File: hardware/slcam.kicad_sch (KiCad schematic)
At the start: 36 parts, among them J1 532610671, J2 Conn_01x08, J3 Conn_01x04, J4 532610371, J5 532610371, U1 STM32F103C8Tx, U2 W25Q128JVS, U3 TCAN330G, U4 TPS2044D, Y1 Crystal_GND24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

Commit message: hardware: Fixing the footprint of the 32 kHz crystal #45
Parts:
- Y2: footprint lib:ECS-.327-12.5-34R-C-TR -> Crystal:Crystal_SMD_MicroCrystal_CC7V-T1A-2Pin_3.2x1.5mm_HandSoldering
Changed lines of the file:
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@@
     (property "Reference" "Y2" (id 0) (at 112.776 118.11 0))
     (property "Value" "Crystal" (id 1) (at 112.776 120.65 0))
-    (property "Footprint" "lib:ECS-.327-12.5-34R-C-TR" (id 2) (at 112.776 125.73 0)
+    (property "Footprint" "Crystal:Crystal_SMD_MicroCrystal_CC7V-T1A-2Pin_3.2x1.5mm_HandSoldering" (id 2) (at 112.776 125.73 0)
       (effects (font (size 1.27 1.27)) hide)
     )
@@
     )
     (path "/c55ccd54-28af-4ab4-883e-eafa97dc9bf8"
-      (reference "Y2") (unit 1) (value "Crystal") (footprint "lib:ECS-.327-12.5-34R-C-TR")
-    )
-  )
+      (reference "Y2") (unit 1) (value "Crystal") (footprint "Crystal:Crystal_SMD_MicroCrystal_CC7V-T1A-2Pin_3.2x1.5mm_HandSoldering")
+    )
+  )

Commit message: hardware: schematics: Adding the partnumbers of some components #52
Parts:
- D1: Partnumber (none) -> LTST-C171GKT
- D2: Partnumber (none) -> LTST-C170KFKT
- J1: Partnumber (none) -> 53261-0671
- J4, J5: Partnumber (none) -> 53261-0371
- U1: Partnumber (none) -> STM32F103C8T6
- U2: Partnumber (none) -> W25Q128JVSIM TR
- U3: Partnumber (none) -> TCAN330GD
- U4: Partnumber (none) -> TPS2044D
- Y1: Partnumber (none) -> ECS-80-10-33-CHN-TR3
- Y2: Partnumber (none) -> ECS-.327-12.5-34S-TR
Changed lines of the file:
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@@
+      (effects (font (size 1.27 1.27)) hide)
+    )
+    (property "Partnumber" "STM32F103C8T6" (id 4) (at 49.53 101.6 0)
       (effects (font (size 1.27 1.27)) hide)
     )
@@
       (effects (font (size 1.27 1.27)) hide)
     )
+    (property "Partnumber" "W25Q128JVSIM TR" (id 4) (at 53.34 248.92 0)
+      (effects (font (size 1.27 1.27)) hide)
+    )
     (pin "1")
     (pin "2")
@@
     )
     (property "Datasheet" "http://www.ti.com/lit/ds/symlink/tps2044.pdf" (id 3) (at 172.72 44.45 0)
+      (effects (font (size 1.27 1.27)) hide)
+    )
+    (property "Partnumber" "TPS2044D" (id 4) (at 173.99 52.07 0)
       (effects (font (size 1.27 1.27)) hide)
     )
@@
       (effects (font (size 1.27 1.27)) hide)
     )
+    (property "Partnumber" "TCAN330GD" (id 4) (at 260.35 252.73 0)
+      (effects (font (size 1.27 1.27)) hide)
+    )
     (pin "1")
     (pin "2")
@@
       (effects (font (size 1.27 1.27)) hide)
     )
+    (property "Partnumber" "ECS-80-10-33-CHN-TR3" (id 4) (at 109.22 86.36 0)
+      (effects (font (size 1.27 1.27)) hide)
+    )
     (pin "1")
     (pin "2")
@@
       (effects (font (size 1.27 1.27)) hide)
     )
+    (property "Partnumber" "53261-0371" (id 4) (at 367.03 55.88 0)
+      (effects (font (size 1.27 1.27)) hide)
+    )
     (pin "1")
     (pin "2")
@@
     )
     (property "Datasheet" "~" (id 3) (at 287.02 143.51 0)
+      (effects (font (size 1.27 1.27)) hide)
+    )
+    (property "Partnumber" "53261-0371" (id 4) (at 287.02 143.51 0)
       (effects (font (size 1.27 1.27)) hide)
     )
@@
     )
     (property "Datasheet" "GREEN" (id 3) (at 212.09 114.808 0))
+    (property "Partnumber" "LTST-C171GKT" (id 4) (at 212.09 111.76 0)
+      (effects (font (size 1.27 1.27)) hide)
+    )
     (pin "1")
     (pin "2")
@@
     )
     (property "Datasheet" "ORANGE" (id 3) (at 212.09 127.508 0))
+    (property "Partnumber" "LTST-C170KFKT" (id 4) (at 212.09 124.46 0)
+      (effects (font (size 1.27 1.27)) hide)
+    )
     (pin "1")
     (pin "2")
@@
     )
     (property "Datasheet" "~" (id 3) (at 370.84 100.33 0)
+      (effects (font (size 1.27 1.27)) hide)
+    )
+    (property "Partnumber" "53261-0671" (id 4) (at 370.84 100.33 0)
       (effects (font (size 1.27 1.27)) hide)
     )
@@
     )
     (property "Datasheet" "http://www.ti.com/lit/ds/symlink/tps2044.pdf" (id 3) (at 222.25 44.45 0)
+      (effects (font (size 1.27 1.27)) hide)
+    )
+    (property "Partnumber" "TPS2044D" (id 4) (at 223.52 52.07 0)
       (effects (font (size 1.27 1.27)) hide)
     )
@@
       (effects (font (size 1.27 1.27)) hide)
     )
+    (property "Partnumber" "ECS-.327-12.5-34S-TR" (id 4) (at 112.776 125.73 0)
+      (effects (font (size 1.27 1.27)) hide)
+    )

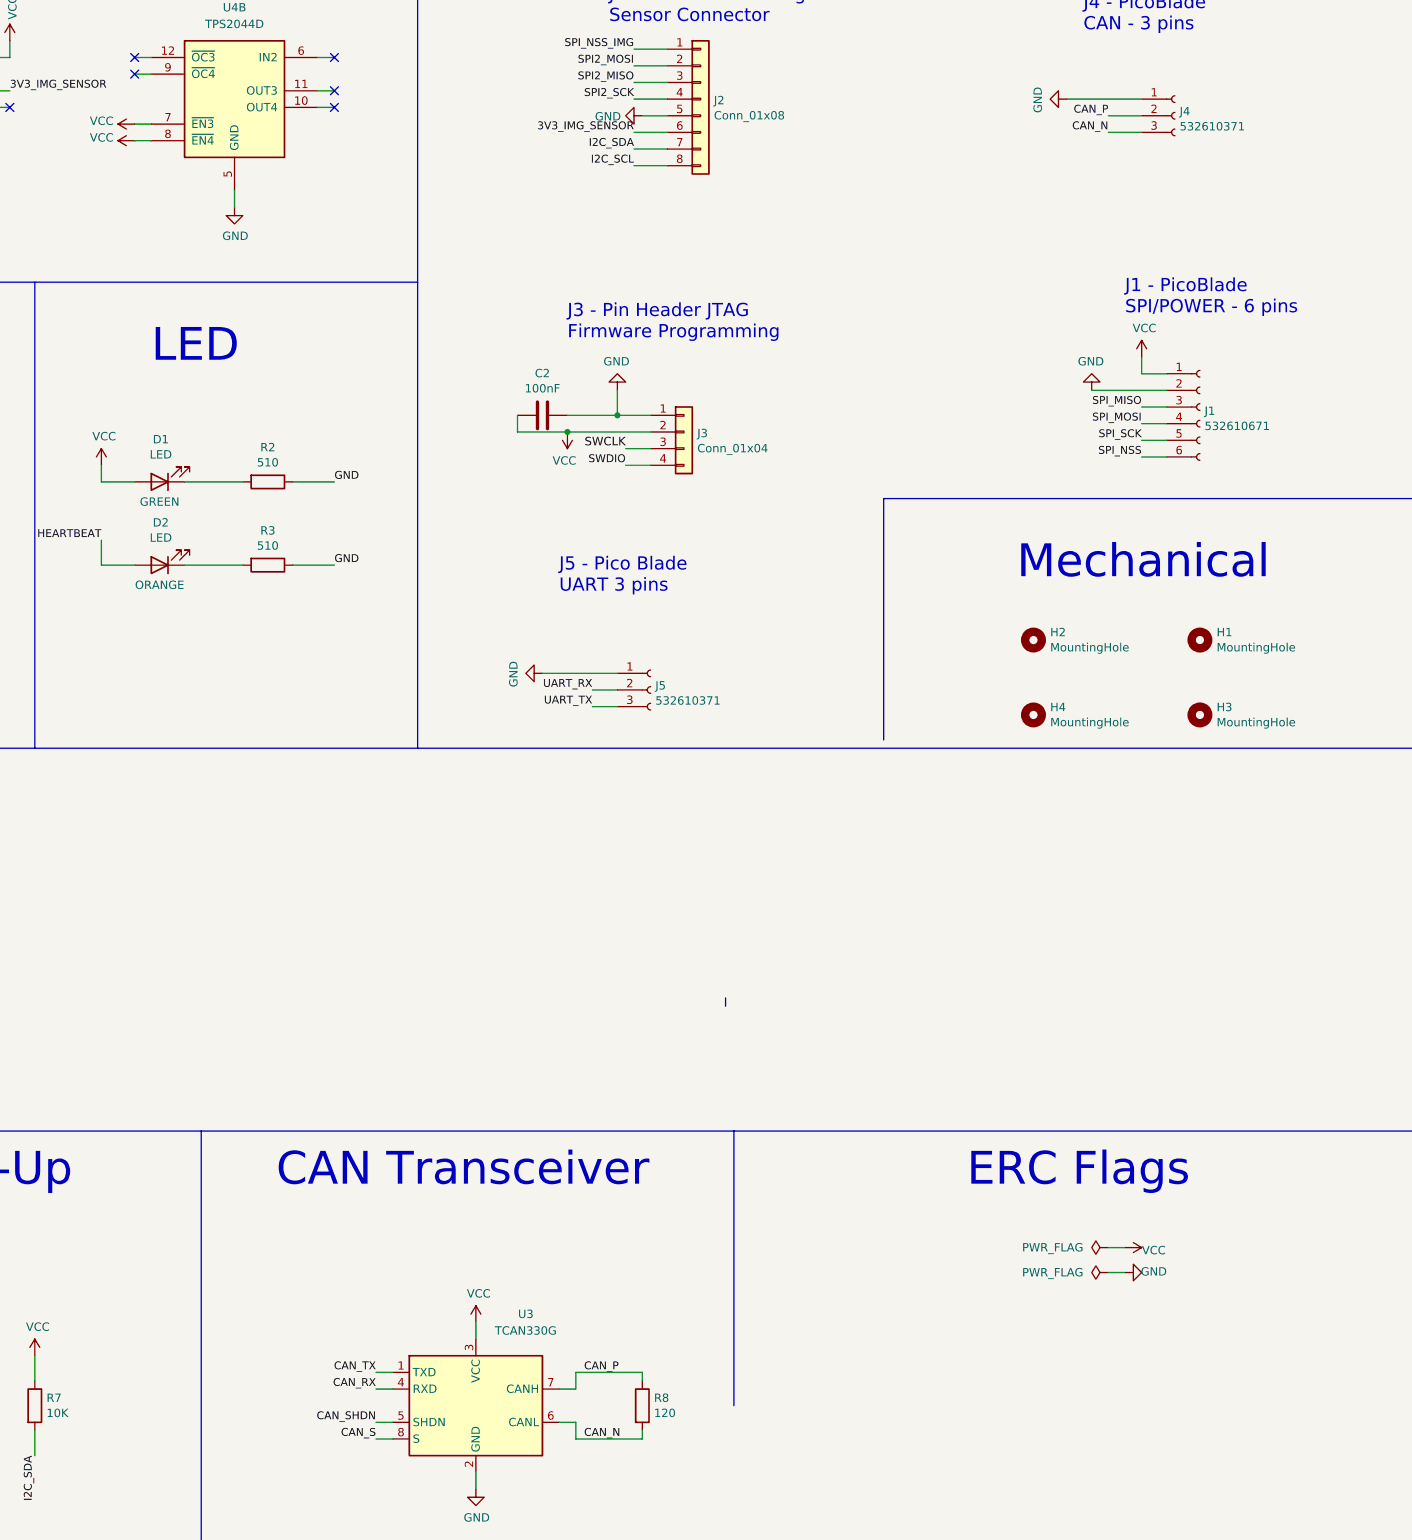
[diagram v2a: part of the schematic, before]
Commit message: hardware: schematics: Adding the partnumbers of components #52
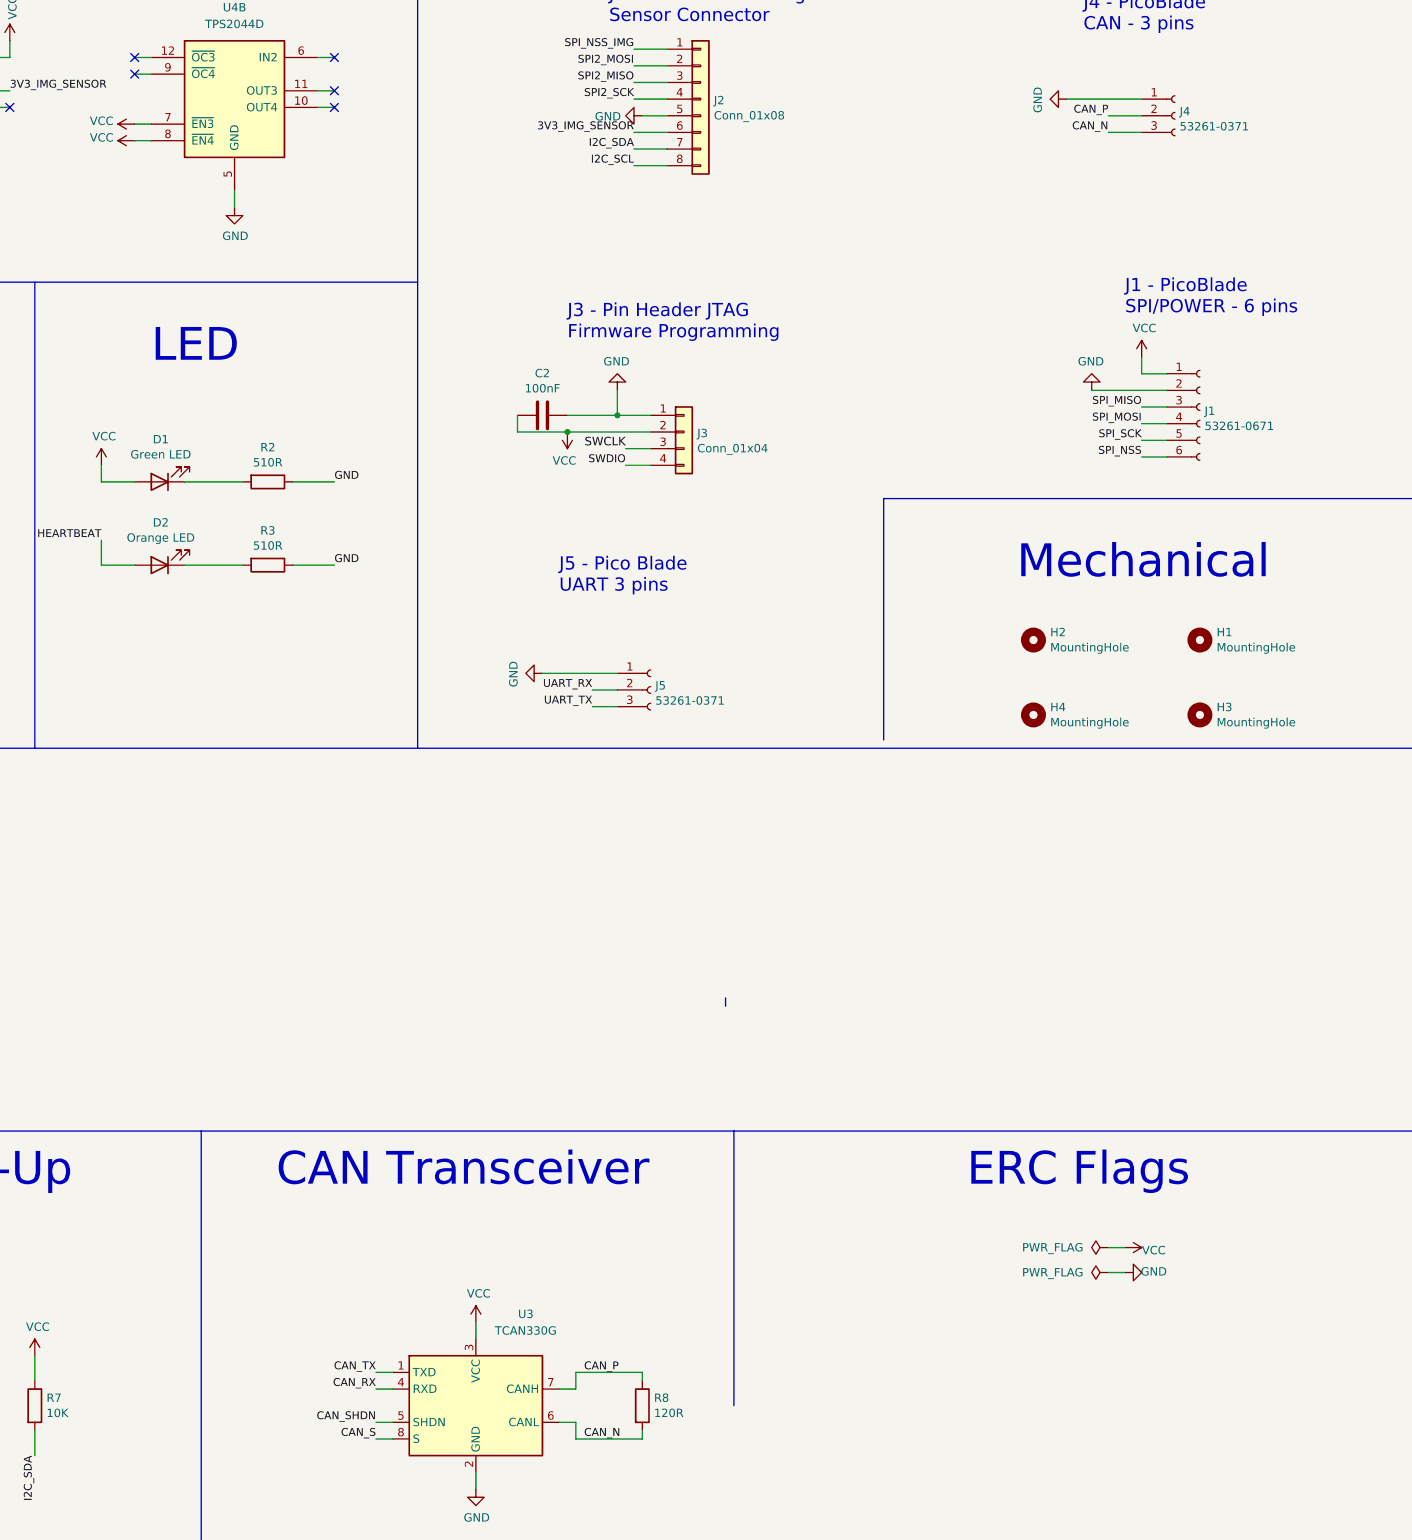
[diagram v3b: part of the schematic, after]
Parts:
- C1: Partnumber (none) -> GCJ188R71E105KA01D
- C10, C9: Partnumber (none) -> CL21C120FBANNNC
- C2: Partnumber (none) -> C0603C104K5RAC3121
- C3, C4, C5, C6: Partnumber (none) -> CL21B103KAANNNC
- C7, C8: Partnumber (none) -> CBR06C200J5GACAUTO
- D1: value LED -> Green LED
- D2: value LED -> Orange LED
- J1: value 532610671 -> 53261-0671
- J2: Partnumber (none) -> SSQ-108-03-G-S
- J3: Partnumber (none) -> 5-146305-4
- J4, J5: value 532610371 -> 53261-0371
- R1, R6, R7: Partnumber (none) -> CRCW080510K0FKEA
- R2, R3: value 510 -> 510R; Partnumber (none) -> MCT06030C5100FP500
- R4, R5: Partnumber (none) -> AC0805FR-13100KL
- R8: value 120 -> 120R; Partnumber (none) -> CRGCQ0805F120R
- R9: Partnumber (none) -> RMCF0805FG1M00

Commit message: hardware: schematics: Adding the partnumbers of components #52
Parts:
- R1, R6, R7: Partnumber CRCW080510K0FKEA -> MCT06030C1002FP500
- R4, R5: Partnumber AC0805FR-13100KL -> MCT0603MC1003FP500
- R8: Partnumber CRGCQ0805F120R -> MCT06030C1200FP500
- R9: Partnumber RMCF0805FG1M00 -> MCT06030C1004FP500
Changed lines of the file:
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@@
       (effects (font (size 1.27 1.27)) hide)
     )
-    (property "Partnumber" "CRCW080510K0FKEA" (id 4) (at 167.64 116.84 0)
+    (property "Partnumber" "MCT06030C1002FP500" (id 4) (at 167.64 116.84 0)
       (effects (font (size 1.27 1.27)) hide)
     )
@@
       (effects (font (size 1.27 1.27)) hide)
     )
-    (property "Partnumber" "CRGCQ0805F120R" (id 4) (at 285.75 252.73 0)
+    (property "Partnumber" "MCT06030C1200FP500" (id 4) (at 285.75 252.73 0)
       (effects (font (size 1.27 1.27)) hide)
     )
@@
       (effects (font (size 1.27 1.27)) hide)
     )
-    (property "Partnumber" "AC0805FR-13100KL" (id 4) (at 107.95 252.73 0)
+    (property "Partnumber" "MCT0603MC1003FP500" (id 4) (at 107.95 252.73 0)
       (effects (font (size 1.27 1.27)) hide)
     )
@@
       (effects (font (size 1.27 1.27)) hide)
     )
-    (property "Partnumber" "AC0805FR-13100KL" (id 4) (at 130.81 252.73 0)
+    (property "Partnumber" "MCT0603MC1003FP500" (id 4) (at 130.81 252.73 0)
       (effects (font (size 1.27 1.27)) hide)
     )
@@
       (effects (font (size 1.27 1.27)) hide)
     )
-    (property "Partnumber" "CRCW080510K0FKEA" (id 4) (at 172.72 252.73 0)
+    (property "Partnumber" "MCT06030C1002FP500" (id 4) (at 172.72 252.73 0)
       (effects (font (size 1.27 1.27)) hide)
     )
@@
       (effects (font (size 1.27 1.27)) hide)
     )
-    (property "Partnumber" "CRCW080510K0FKEA" (id 4) (at 193.04 252.73 0)
+    (property "Partnumber" "MCT06030C1002FP500" (id 4) (at 193.04 252.73 0)
       (effects (font (size 1.27 1.27)) hide)
     )
@@
       (effects (font (size 1.27 1.27)) hide)
     )
-    (property "Partnumber" "RMCF0805FG1M00" (id 4) (at 109.22 101.6 0)
-      (effects (font (size 1.27 1.27)) hide)
-    )
+    (property "Partnumber" "MCT06030C1004FP500" (id 4) (at 109.22 101.6 0)
+      (effects (font (size 1.27 1.27)) hide)
+    )

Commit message: hardware: Fixing the partnumber of C3, C4, C5 and C6
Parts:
- C3, C4, C5, C6: Partnumber CL21B103KAANNNC -> VJ0603Y103KXJAC31X
- D1: Partnumber LTST-C171GKT -> 150060VS75003
- D2: Partnumber LTST-C170KFKT -> CSL1901DW1
- H1, H2, H3, H4: now left out of the parts list
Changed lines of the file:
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@@
   (title_block
     (title "SLCam")
-    (date "2023-04-29")
+    (date "2023-05-09")
     (rev "v0.2")
     (company "Space Technology Research Laboratory - SpaceLab")
@@
   )
   (symbol (lib_id "Mechanical:MountingHole") (at 345.44 135.89 0) (unit 1)
-    (in_bom yes) (on_board yes)
+    (in_bom no) (on_board yes)
     (property "Reference" "H2" (id 0) (at 347.98 134.7216 0)
       (effects (font (size 1.27 1.27)) (justify left))
@@
   )
   (symbol (lib_id "Mechanical:MountingHole") (at 370.84 135.89 0) (unit 1)
-    (in_bom yes) (on_board yes)
+    (in_bom no) (on_board yes)
     (property "Reference" "H1" (id 0) (at 373.38 134.7216 0)
       (effects (font (size 1.27 1.27)) (justify left))
@@
   )
   (symbol (lib_id "Mechanical:MountingHole") (at 370.84 147.32 0) (unit 1)
-    (in_bom yes) (on_board yes)
+    (in_bom no) (on_board yes)
     (property "Reference" "H3" (id 0) (at 373.38 146.1516 0)
       (effects (font (size 1.27 1.27)) (justify left))
@@
   )
   (symbol (lib_id "Mechanical:MountingHole") (at 345.44 147.32 0) (unit 1)
-    (in_bom yes) (on_board yes)
+    (in_bom no) (on_board yes)
     (property "Reference" "H4" (id 0) (at 347.98 146.1516 0)
       (effects (font (size 1.27 1.27)) (justify left))
@@
       (effects (font (size 1.27 1.27)) hide)
     )
-    (property "Partnumber" "LTST-C171GKT" (id 4) (at 212.09 111.76 0)
+    (property "Partnumber" "150060VS75003" (id 4) (at 212.09 111.76 0)
       (effects (font (size 1.27 1.27)) hide)
     )
@@
       (effects (font (size 1.27 1.27)) hide)
     )
-    (property "Partnumber" "LTST-C170KFKT" (id 4) (at 212.09 124.46 0)
+    (property "Partnumber" "CSL1901DW1" (id 4) (at 212.09 124.46 0)
       (effects (font (size 1.27 1.27)) hide)
     )
@@
       (effects (font (size 1.27 1.27)) hide)
     )
-    (property "Partnumber" "CL21B103KAANNNC" (id 4) (at 44.45 179.07 0)
+    (property "Partnumber" "VJ0603Y103KXJAC31X" (id 4) (at 44.45 179.07 0)
       (effects (font (size 1.27 1.27)) hide)
     )
@@
       (effects (font (size 1.27 1.27)) hide)
     )
-    (property "Partnumber" "CL21B103KAANNNC" (id 4) (at 58.42 179.07 0)
+    (property "Partnumber" "VJ0603Y103KXJAC31X" (id 4) (at 58.42 179.07 0)
       (effects (font (size 1.27 1.27)) hide)
     )
@@
       (effects (font (size 1.27 1.27)) hide)
     )
-    (property "Partnumber" "CL21B103KAANNNC" (id 4) (at 73.66 179.07 0)
+    (property "Partnumber" "VJ0603Y103KXJAC31X" (id 4) (at 73.66 179.07 0)
       (effects (font (size 1.27 1.27)) hide)
     )
@@
       (effects (font (size 1.27 1.27)) hide)
     )
-    (property "Partnumber" "CL21B103KAANNNC" (id 4) (at 30.48 179.07 0)
-      (effects (font (size 1.27 1.27)) hide)
-    )
+    (property "Partnumber" "VJ0603Y103KXJAC31X" (id 4) (at 30.48 179.07 0)
+      (effects (font (size 1.27 1.27)) hide)
+    )
